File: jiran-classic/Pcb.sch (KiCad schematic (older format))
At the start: 133 parts, among them J1 TRRS, Q1 2N7002, SW1 SW_Push, SW10 SW_Push, SW11 SW_Push, SW12 SW_Push, SW13 SW_Push, SW14 SW_Push, SW15 SW_Push, SW16 SW_Push, SW17 SW_Push, SW18 SW_Push, SW19 SW_Push, SW2 SW2, SW20 SW_Push, SW21 SW_Push, SW22 SW_Push, SW23 SW_Push, SW24 SW_Push, SW25 SW_Push, SW26 SW_Push, SW27 SW_Push, SW28 SW_Push, SW29 SW_Push, SW3 SW_Push, SW4 SW_Push, SW5 SW_Push, SW6 SW_Push, SW7 SW_Push, SW8 SW_Push, SW9 SW_Push, U1 ProMicro

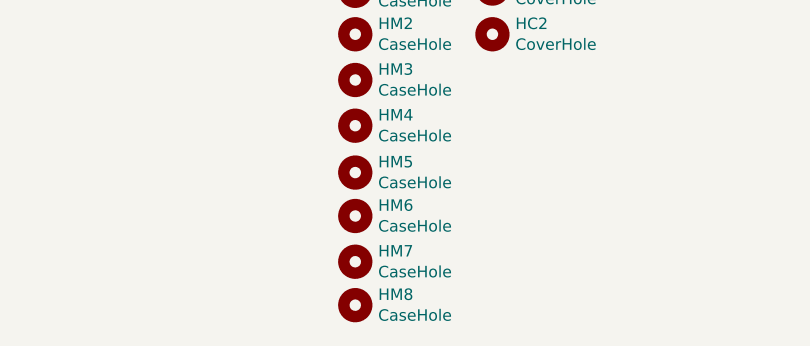
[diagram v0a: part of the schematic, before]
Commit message: Replace some footprint
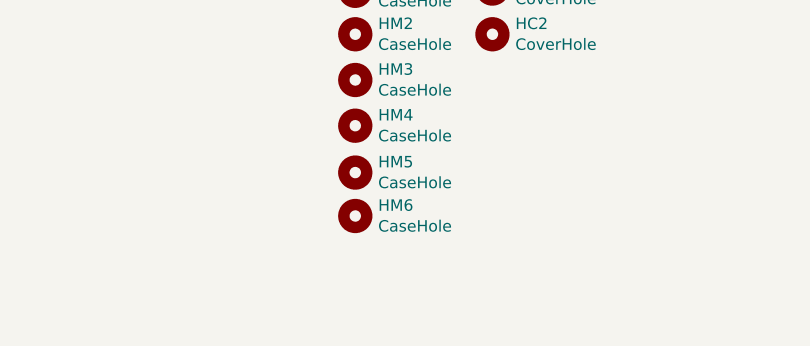
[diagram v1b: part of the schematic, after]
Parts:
- removed HM7, HM8: CaseHole, Used_Footprints:Hole_Mount_M4, symbol Mechanical:MountingHole
- D1, D10, D11, D12, D13, D14, D15, D16, D17, D18, D19, D2, D20, D21, D22, D23, D24, D25, D26, D27, D28, D3, D4, D5, D6, D7, D8, D9: footprint Used_Footprints:Diode_Hybrid_SOD-123 -> used_footprints:Diode_Hybrid_SOD-123
- D29, D30, D31, D32, D33, D34, D35, D36, D37, D38, D39, D40, D41, D42, D43, D44, D45, D46, D47, D48, D49, D50, D51, D52, D53, D54, D55, D56: footprint Used_Footprints:LED_THT_1.8mm -> used_footprints:LED_THT
- HC1, HC2: footprint Used_Footprints:Hole_Cover_M2 -> used_footprints:Hole_Cover_M2
- HM1, HM2, HM3, HM4, HM5, HM6: footprint Used_Footprints:Hole_Mount_M4 -> used_footprints:Hole_Mount_M4
- J1: footprint Used_Footprints:TRSS_DUAL_THT -> used_footprints:TRSS_DUAL_THT
- JP1, JP2, JP3, JP4: footprint Used_Footprints:Jumper_SMD -> used_footprints:Jumper_SMD
- Q1: footprint Used_Footprints:Mosfet_SMD_Dual_SOT-23 -> used_footprints:Mosfet_SMD_Dual_SOT-23
- R1, R10, R11, R12, R13, R14, R15, R16, R17, R18, R19, R2, R20, R21, R22, R23, R24, R25, R26, R27, R28, R29, R3, R30, R31, R4, R5, R6, R7, R8, R9: footprint Used_Footprints:Resistor_Hybrid_1205 -> used_footprints:Resistor_Hybrid_1205
- SW1, SW10, SW11, SW12, SW13, SW14, SW15, SW16, SW17, SW18, SW19, SW20, SW21, SW22, SW23, SW24, SW25, SW26, SW27, SW28, SW3, SW4, SW5, SW6, SW7, SW8, SW9: footprint Used_Footprints:Switch_MxAlpsChoc_MillMax_1u -> used_footprints:Switch_MxAlpsChoc_MillMax_1u
- SW2: value SW2 -> SW_Push; footprint Used_Footprints:Switch_MxAlpsChoc_MillMax_1u -> used_footprints:Switch_MxAlpsChoc_MillMax_1u
- SW29: footprint Used_Footprints:Switch_Reset_THT -> used_footprints:Switch_Reset_THT
- U1: footprint Used_Footprints:ProMicro_Dual -> used_footprints:ProMicro_Dual

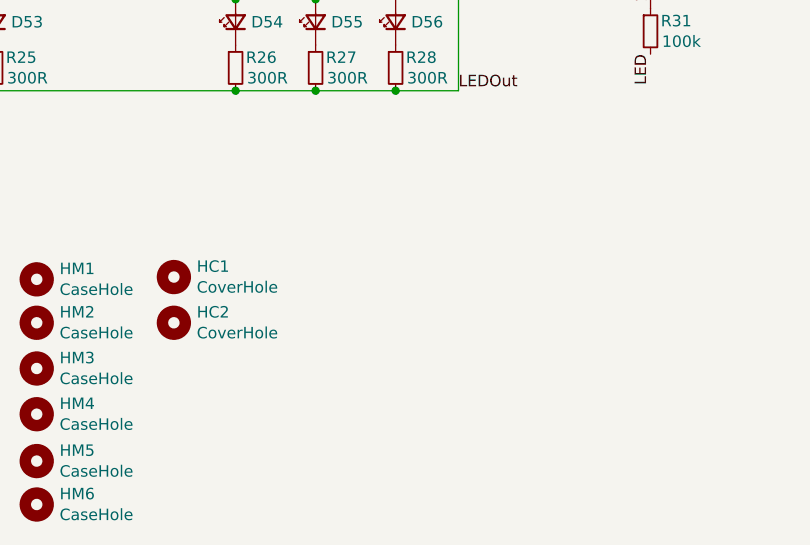
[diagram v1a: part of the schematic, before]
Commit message: Add logo as symbol
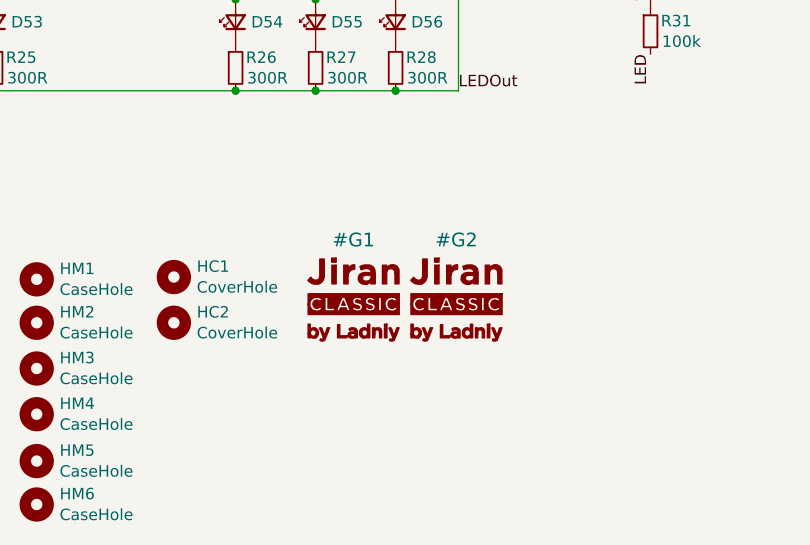
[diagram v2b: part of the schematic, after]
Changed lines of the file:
@@
 Wire Wire Line
 	9360 1785 9360 2285
+$Comp
+L jiran:LOGO #G1
+U 1 1 5FA09AD8
+P 8900 4250
+F 0 "#G1" H 8901 4562 60  0000 C CNN
+F 1 "LOGO" H 8900 4050 60  0001 C CNN
+F 2 "" H 8900 4250 50  0001 C CNN
+F 3 "" H 8900 4250 50  0001 C CNN
+	1    8900 4250
+	1    0    0    -1
+$EndComp
+$Comp
+L jiran:LOGO #G2
+U 1 1 5FA0B668
+P 9350 4250
+F 0 "#G2" H 9351 4562 60  0000 C CNN
+F 1 "LOGO" H 9350 4050 60  0001 C CNN
+F 2 "" H 9350 4250 50  0001 C CNN
+F 3 "" H 9350 4250 50  0001 C CNN
+	1    9350 4250
+	1    0    0    -1
+$EndComp
 $EndSCHEMATC

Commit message: Assign logo symbols with logo footprints
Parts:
- added G1, G2: LOGO, used_footprints:Silk_Logotype, symbol jiran:LOGO
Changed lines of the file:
@@
 	9360 1785 9360 2285
 $Comp
-L jiran:LOGO #G1
+L jiran:LOGO G1
 U 1 1 5FA09AD8
 P 8900 4250
-F 0 "#G1" H 8901 4562 60  0000 C CNN
+F 0 "G1" H 8850 4550 60  0000 L CNN
 F 1 "LOGO" H 8900 4050 60  0001 C CNN
-F 2 "" H 8900 4250 50  0001 C CNN
+F 2 "used_footprints:Silk_Logotype" H 8900 4250 50  0001 C CNN
 F 3 "" H 8900 4250 50  0001 C CNN
 	1    8900 4250
@@
 $EndComp
 $Comp
-L jiran:LOGO #G2
+L jiran:LOGO G2
 U 1 1 5FA0B668
 P 9350 4250
-F 0 "#G2" H 9351 4562 60  0000 C CNN
+F 0 "G2" H 9300 4550 60  0000 L CNN
 F 1 "LOGO" H 9350 4050 60  0001 C CNN
-F 2 "" H 9350 4250 50  0001 C CNN
+F 2 "used_footprints:Silk_Logotype" H 9350 4250 50  0001 C CNN
 F 3 "" H 9350 4250 50  0001 C CNN
 	1    9350 4250

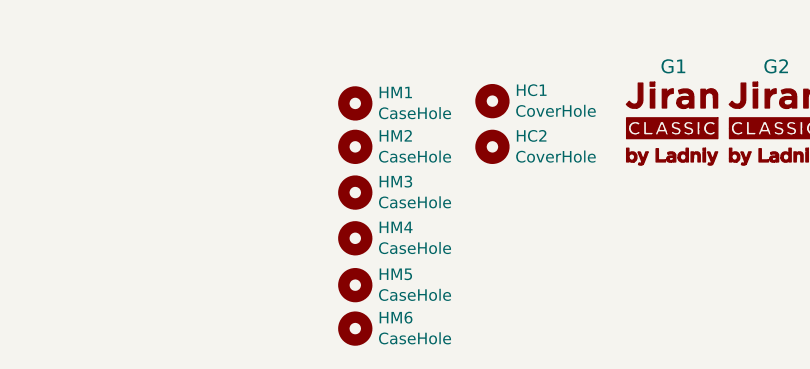
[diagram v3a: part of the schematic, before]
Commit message: Remove one hole mount (HM3)
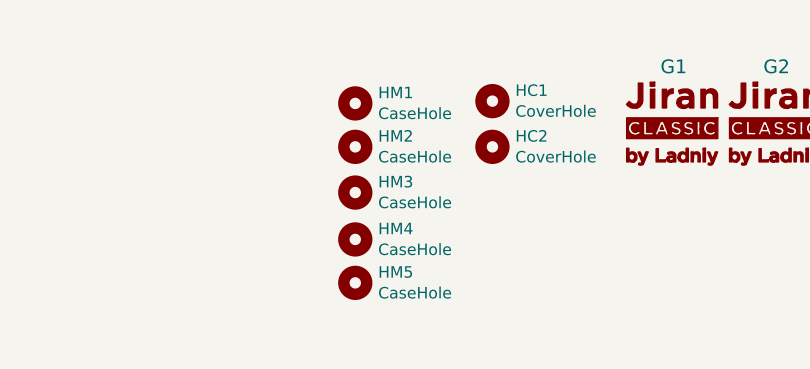
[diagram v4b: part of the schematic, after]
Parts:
- removed HM3: CaseHole, used_footprints:Hole_Mount_M4, symbol Mechanical:MountingHole
- renumbered HM4 to HM3, HM5 to HM4, HM6 to HM5
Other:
- moved on the sheet: HM3, HM4, HM5
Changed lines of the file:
@@
 $Comp
 L Mechanical:MountingHole HM3
-U 1 1 5DC0F92C
+U 1 1 5DC14B86
 P 7515 4500
 F 0 "HM3" H 7615 4546 50  0000 L CNN
@@
 $Comp
 L Mechanical:MountingHole HM4
-U 1 1 5DC14B86
-P 7515 4700
-F 0 "HM4" H 7615 4746 50  0000 L CNN
-F 1 "CaseHole" H 7615 4655 50  0000 L CNN
-F 2 "used_footprints:Hole_Mount_M4" H 7515 4700 50  0001 C CNN
-F 3 "~" H 7515 4700 50  0001 C CNN
-	1    7515 4700
+U 1 1 5DC1BC70
+P 7515 4705
+F 0 "HM4" H 7615 4751 50  0000 L CNN
+F 1 "CaseHole" H 7615 4660 50  0000 L CNN
+F 2 "used_footprints:Hole_Mount_M4" H 7515 4705 50  0001 C CNN
+F 3 "~" H 7515 4705 50  0001 C CNN
+	1    7515 4705
 	1    0    0    -1
 $EndComp
 $Comp
 L Mechanical:MountingHole HM5
-U 1 1 5DC1BC70
-P 7515 4905
-F 0 "HM5" H 7615 4951 50  0000 L CNN
-F 1 "CaseHole" H 7615 4860 50  0000 L CNN
-F 2 "used_footprints:Hole_Mount_M4" H 7515 4905 50  0001 C CNN
-F 3 "~" H 7515 4905 50  0001 C CNN
-	1    7515 4905
+U 1 1 5DC1BC76
+P 7515 4895
+F 0 "HM5" H 7615 4941 50  0000 L CNN
+F 1 "CaseHole" H 7615 4850 50  0000 L CNN
+F 2 "used_footprints:Hole_Mount_M4" H 7515 4895 50  0001 C CNN
+F 3 "~" H 7515 4895 50  0001 C CNN
+	1    7515 4895
 	1    0    0    -1
 $EndComp
-$Comp
-L Mechanical:MountingHole HM6
-U 1 1 5DC1BC76
-P 7515 5095
-F 0 "HM6" H 7615 5141 50  0000 L CNN
-F 1 "CaseHole" H 7615 5050 50  0000 L CNN
-F 2 "used_footprints:Hole_Mount_M4" H 7515 5095 50  0001 C CNN
-F 3 "~" H 7515 5095 50  0001 C CNN
-	1    7515 5095
-	1    0    0    -1
-$EndComp
